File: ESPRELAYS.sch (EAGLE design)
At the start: 52 parts, among them IC1 ESP12SMT, J1 2.1MM DC Jack, K1 HE751, K2 HE751, K3 HE751, K4 HE751, Q1 2N7002, Q2 2N7002, Q3 2N7002, Q4 2N7002

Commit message: Added SIP reed relays
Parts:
- added D5, D6: (no value), SparkFun:DIODESMA
- added H8, H9: (no value), freetronics-jon:M02PTH
- added K5, K6: REED, relay:REED
- K1, K2, K3, K4: value HE751 -> REED; device relay:HE751 -> relay:REED
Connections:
- new net N$15: H8.1, K42.S
- new net N$16: H8.2, K42.P
- new net N$17: H9.1, K62.S
- new net N$18: H9.2, K62.P
- new net OUT5: D5.A, K41.+
- new net OUT6: D6.A, K61.+
- net 5V: now also D5.C, D6.C, K11.-, K21.-, K31.-, K41.-, K51.-, K61.-; no longer K11.1, K21.1, K31.1, K41.1
- net N$12: now also K52.P; no longer K42.S
- net N$13: now also K32.S; no longer K32.P
- net N$14: now also K32.P; no longer K32.S
- net N$3: now also K12.S; no longer K12.P
- net N$5: now also K12.P; no longer K12.S
- net N$6: now also K22.S; no longer K22.P
- net N$8: now also K52.S; no longer K42.P
- net N$9: now also K22.P; no longer K22.S
- net OUT1: now also K51.+; no longer K41.2
- net OUT2: now also K11.+; no longer K11.2
- net OUT3: now also K21.+; no longer K21.2
- net OUT4: now also K31.+; no longer K31.2
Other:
- moved on the sheet: K1, K2, K3, K4

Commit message: Routing for v1.0 release
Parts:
- removed H2: (no value), freetronics-jon:M02PTH
- removed H3: (no value), freetronics-jon:M04PTH
- added JP1: (no value), freetronics-jon:M03PTH
- added LED7, LED8: RED, freetronics-master-v1:LED0603
- added Q5, Q6: 2N7002, freetronics-master-v1:MOSFET-NCHANNELSMD
- added R19, R20, R22, R23: 1K, freetronics-master-v1:RESISTOR0603
- added R21, R5: 10K, freetronics-master-v1:RESISTOR0603
- D1, D2, D3, D4, D5, D6: value (none) -> 1N4004
- LED2: value CH2/RED -> RED
- LED3: value CH3/RED -> RED
- LED4: value CH4/RED -> RED
- LED5: value CH1/RED -> RED
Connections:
- new net N$19: Q5.G, R19.1, R5.2
- new net N$20: LED7.C, R20.1
- new net N$22: Q6.G, R21.2, R22.1
- new net N$26: LED8.C, R23.1
- net 3.3V: now also JP1.2; no longer H2.1, LED2.A, LED3.A, LED4.A, LED5.A
- net 5V: now also JP1.1, LED2.A, LED3.A, LED4.A, LED5.A, LED7.A, LED8.A
- net GND: now also JP1.3, Q5.S, Q6.S, R21.1, R5.1; no longer H2.2
- net GPIO15: now also R22.2
- net GPIO16: now also R19.2
- net OUT1: no longer H3.1
- net OUT2: no longer H3.2
- net OUT3: no longer H3.3
- net OUT4: no longer H3.4
- net OUT5: now also Q5.D, R20.2
- net OUT6: now also Q6.D, R23.2
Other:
- note added: "5"
- note added: "6"
- note added: "Do not place"
- note added: "Output 1: GPIO12 Output 2: GPIO13 Output 3: GPIO14 Output 4: GPIO5 Output 5: GPIO16 Output 6: GPIO15"
- note added: "Output 5"
- note added: "Output 6"
- note added: "SKU: ESPRELAYS"
- note added: "SuperHouse Automation ESP8266 Relays"
- note added: "V1.0 (2019-04-11)"
- note added: "www.superhouse.tv/esprelays"
- note removed: "Output 1: GPIO12 Output 2: GPIO13 Output 3: GPIO14 Output 4: GPIO5"
- note removed: "SKU: ESPREMOTE"
- note removed: "SuperHouse Automation ESP8266 Remote"
- note removed: "Tx Buttons"
- note removed: "V3.1 (2018-03-28)"
- note removed: "www.superhouse.tv/espremote"
- moved on the sheet: D1, D2, D3, D4, D5, D6, H4, H5, H6, H7, H8, H9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

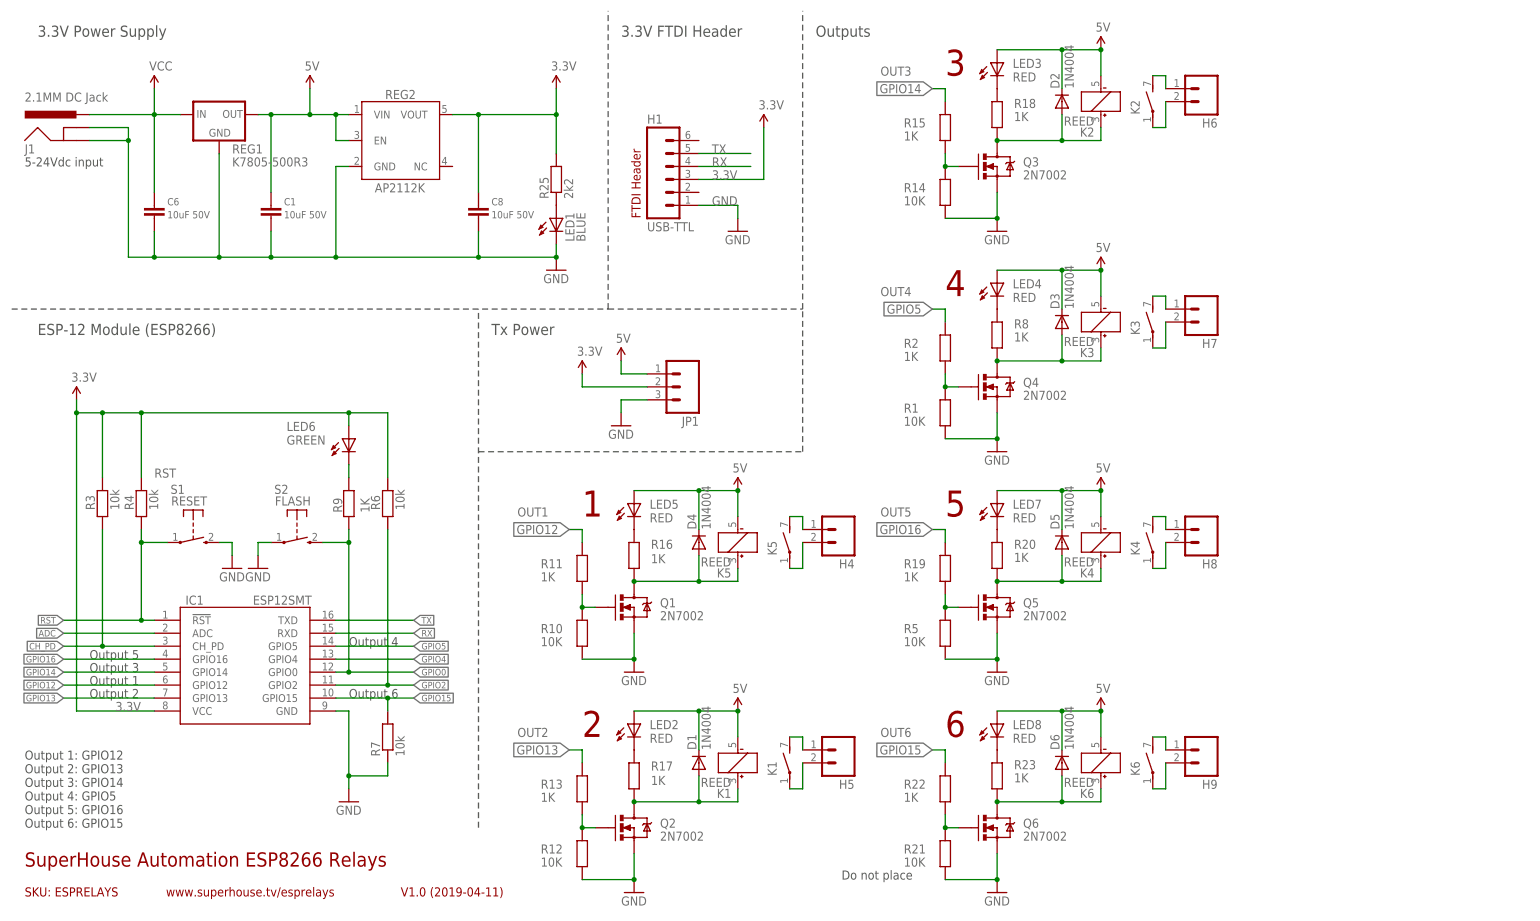
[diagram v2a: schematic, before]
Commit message: Changed output pins to avoid GPIO16 because it pulses on startup. v1.1 release
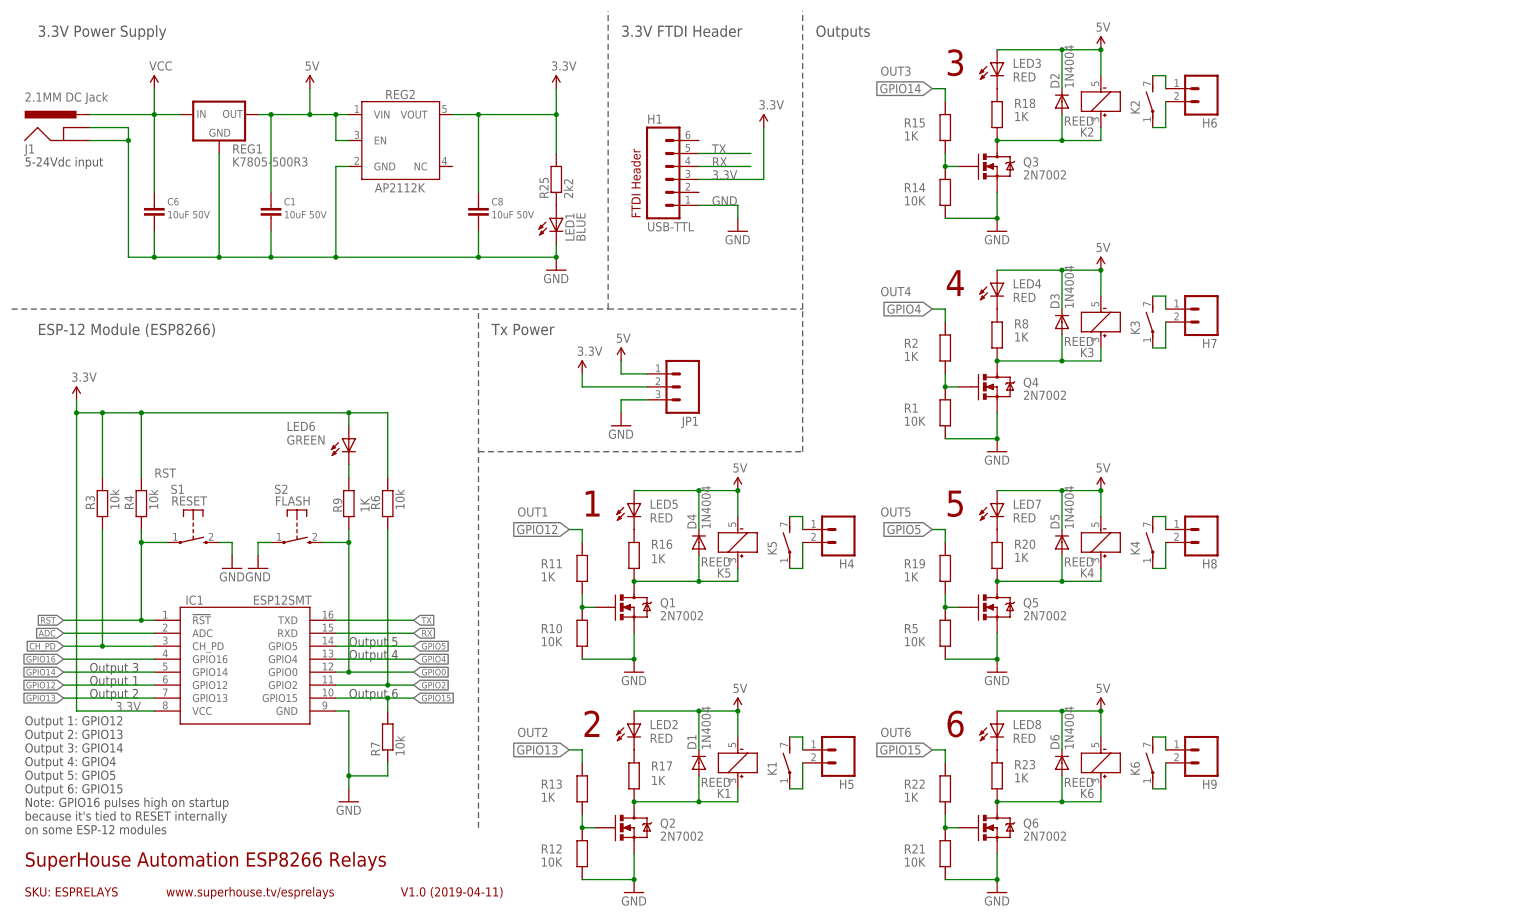
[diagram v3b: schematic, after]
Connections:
- net GPIO16: no longer R19.2
- net GPIO4: now also R2.2
- net GPIO5: now also R19.2; no longer R2.2
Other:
- note added: "Output 1: GPIO12 Output 2: GPIO13 Output 3: GPIO14 Output 4: GPIO4 Output 5: GPIO5 Output 6: GPIO15 Note: GPIO16 pulses high on startup because it's tied to RESET internally on some ESP-12 modules"
- note removed: "Do not place"
- note removed: "Output 1: GPIO12 Output 2: GPIO13 Output 3: GPIO14 Output 4: GPIO5 Output 5: GPIO16 Output 6: GPIO15"
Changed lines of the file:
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@@
 <?xml version="1.0" encoding="utf-8"?>
 <!DOCTYPE eagle SYSTEM "eagle.dtd">
-<eagle version="9.3.1">
+<eagle version="9.3.0">
 <drawing>
 <settings>
-<setting alwaysvectorfont="yes"/>
+<setting alwaysvectorfont="no"/>
 <setting keepoldvectorfont="yes"/>
 <setting verticaltext="up"/>
@@
 <text x="124.46" y="175.26" size="2.1844" layer="97" font="vector" ratio="15">3.3V FTDI Header</text>
 <text x="7.62" y="149.86" size="1.778" layer="97" font="vector" ratio="10">5-24Vdc input</text>
-<text x="7.62" y="20.32" size="1.778" layer="97" font="vector" ratio="10">Output 1: GPIO12
+<text x="7.62" y="19.05" size="1.778" layer="97" font="vector" ratio="10">Output 1: GPIO12
 Output 2: GPIO13
 Output 3: GPIO14
-Output 4: GPIO5
-Output 5: GPIO16
-Output 6: GPIO15</text>
+Output 4: GPIO4
+Output 5: GPIO5
+Output 6: GPIO15
+Note: GPIO16 pulses high on startup
+because it's tied to RESET internally
+on some ESP-12 modules</text>
 <text x="20.32" y="48.26" size="1.778" layer="97">Output 1</text>
 <text x="20.32" y="45.72" size="1.778" layer="97">Output 2</text>
 <text x="20.32" y="50.8" size="1.778" layer="97">Output 3</text>
-<text x="71.12" y="55.88" size="1.778" layer="97">Output 4</text>
+<text x="71.12" y="53.34" size="1.778" layer="97">Output 4</text>
 <text x="187.96" y="81.28" size="5.08" layer="94" ratio="12">5</text>
 <text x="187.96" y="38.1" size="5.08" layer="94" ratio="12">6</text>
-<text x="20.32" y="53.34" size="1.778" layer="97">Output 5</text>
+<text x="71.12" y="55.88" size="1.778" layer="97">Output 5</text>
 <text x="71.12" y="45.72" size="1.778" layer="97">Output 6</text>
 <wire x1="96.52" y1="20.32" x2="96.52" y2="121.92" width="0.254" layer="97" style="longdash"/>
@@
 <wire x1="160.02" y1="93.98" x2="160.02" y2="121.92" width="0.254" layer="97" style="longdash"/>
 <text x="99.06" y="116.84" size="2.1844" layer="97" font="vector" ratio="15">Tx Power</text>
-<text x="167.64" y="10.16" size="1.778" layer="97">Do not place</text>
 </plain>
 <instances>
@@
 </segment>
 <segment>
+<wire x1="187.96" y1="76.2" x2="187.96" y2="78.74" width="0.1524" layer="91"/>
+<wire x1="187.96" y1="78.74" x2="185.42" y2="78.74" width="0.1524" layer="91"/>
+<label x="185.42" y="78.74" size="1.778" layer="95" rot="R180" xref="yes"/>
+<pinref part="R19" gate="G$1" pin="2"/>
+</segment>
+</net>
+<net name="GPIO4" class="0">
+<segment>
+<pinref part="IC1" gate="G$1" pin="GPIO4"/>
+<wire x1="68.58" y1="53.34" x2="83.82" y2="53.34" width="0.1524" layer="91"/>
+<label x="83.82" y="53.34" size="1.27" layer="95" xref="yes"/>
+</segment>
+<segment>
 <pinref part="R2" gate="G$1" pin="2"/>
 <wire x1="187.96" y1="119.38" x2="187.96" y2="121.92" width="0.1524" layer="91"/>
 <wire x1="187.96" y1="121.92" x2="185.42" y2="121.92" width="0.1524" layer="91"/>
 <label x="185.42" y="121.92" size="1.778" layer="95" rot="R180" xref="yes"/>
-</segment>
-</net>
-<net name="GPIO4" class="0">
-<segment>
-<pinref part="IC1" gate="G$1" pin="GPIO4"/>
-<wire x1="68.58" y1="53.34" x2="83.82" y2="53.34" width="0.1524" layer="91"/>
-<label x="83.82" y="53.34" size="1.27" layer="95" xref="yes"/>
 </segment>
 </net>
@@
 <label x="15.24" y="53.34" size="1.27" layer="95" rot="R180" xref="yes"/>
 </segment>
-<segment>
-<wire x1="187.96" y1="76.2" x2="187.96" y2="78.74" width="0.1524" layer="91"/>
-<wire x1="187.96" y1="78.74" x2="185.42" y2="78.74" width="0.1524" layer="91"/>
-<label x="185.42" y="78.74" size="1.778" layer="95" rot="R180" xref="yes"/>
-<pinref part="R19" gate="G$1" pin="2"/>
-</segment>
 </net>

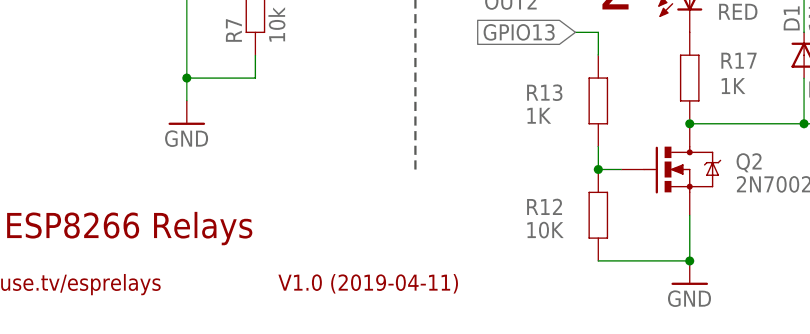
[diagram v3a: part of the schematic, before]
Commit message: Fixed revision number in schematic
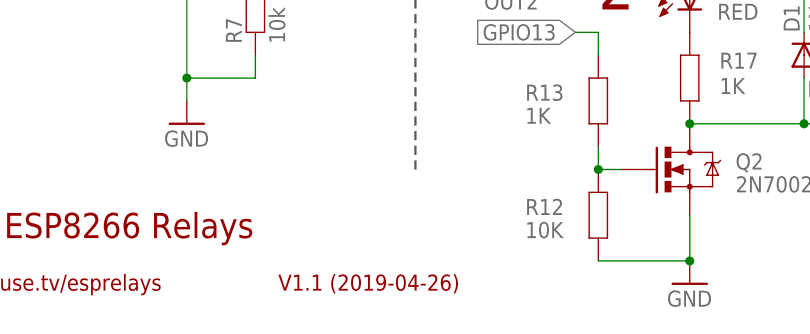
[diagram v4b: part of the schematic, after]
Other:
- note added: "V1.1 (2019-04-26)"
- note removed: "V1.0 (2019-04-11)"
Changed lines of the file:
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@@
 <?xml version="1.0" encoding="utf-8"?>
 <!DOCTYPE eagle SYSTEM "eagle.dtd">
-<eagle version="9.3.0">
+<eagle version="9.4.0">
 <drawing>
 <settings>
@@
 <text x="7.62" y="6.858" size="1.778" layer="94">SKU: ESPRELAYS</text>
 <text x="7.62" y="12.7" size="2.794" layer="94">SuperHouse Automation ESP8266 Relays</text>
-<text x="81.28" y="6.858" size="1.778" layer="94">V1.0 (2019-04-11)</text>
+<text x="81.28" y="6.858" size="1.778" layer="94">V1.1 (2019-04-26)</text>
 <text x="35.306" y="6.858" size="1.778" layer="94">www.superhouse.tv/esprelays</text>
 <frame x1="5.08" y1="5.08" x2="109.22" y2="17.78" columns="0" rows="0" layer="94" border-left="no" border-top="no" border-right="no" border-bottom="no"/>

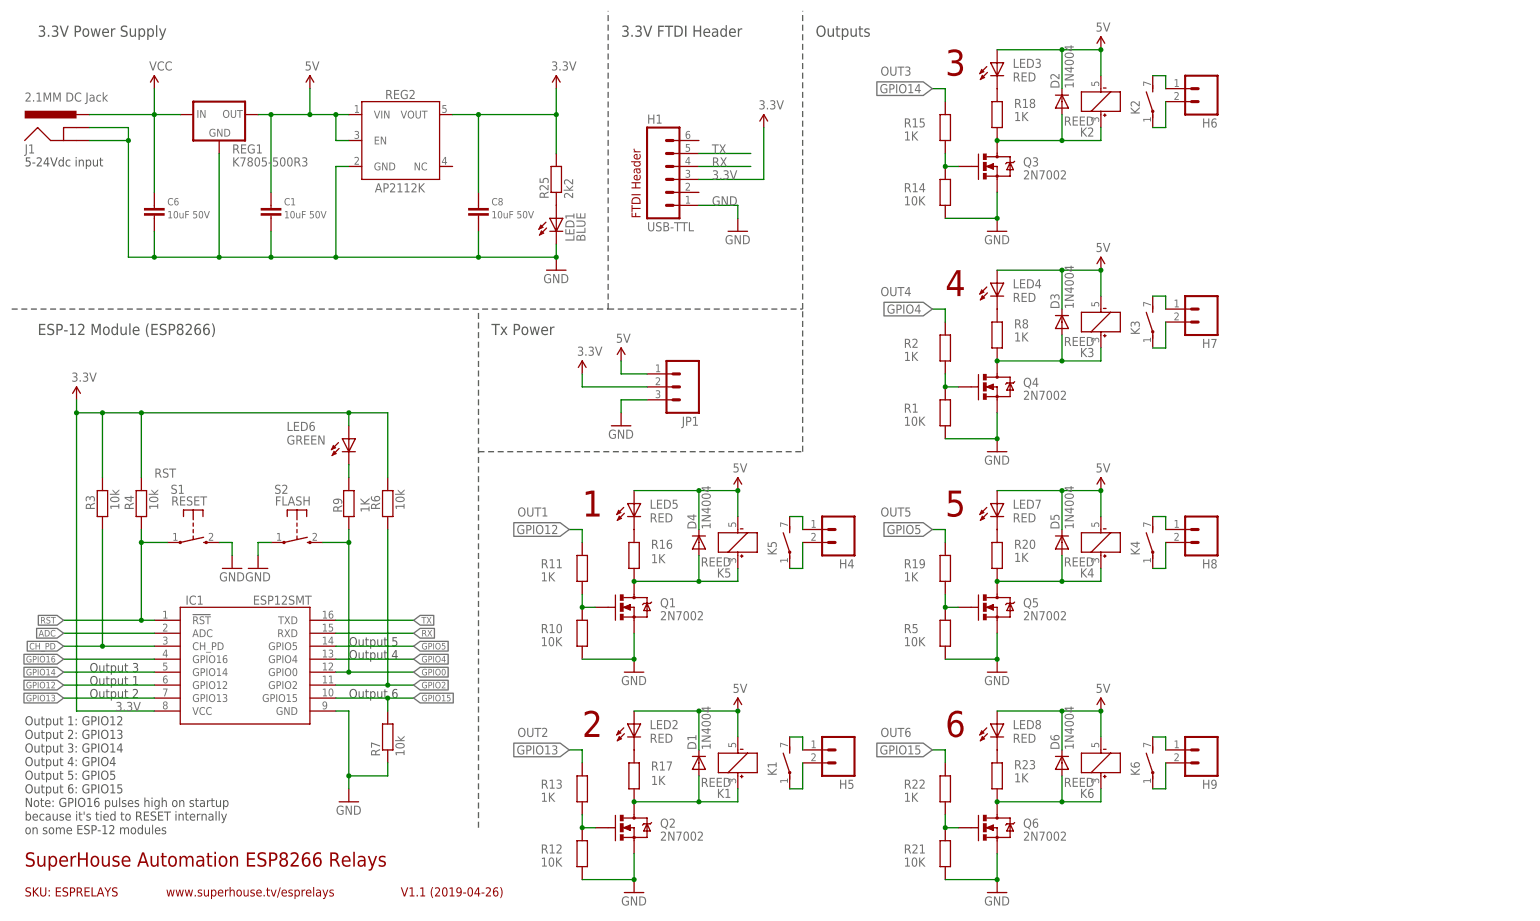
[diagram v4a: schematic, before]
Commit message: Replaced most parts using SuperHouse library to add 3D models
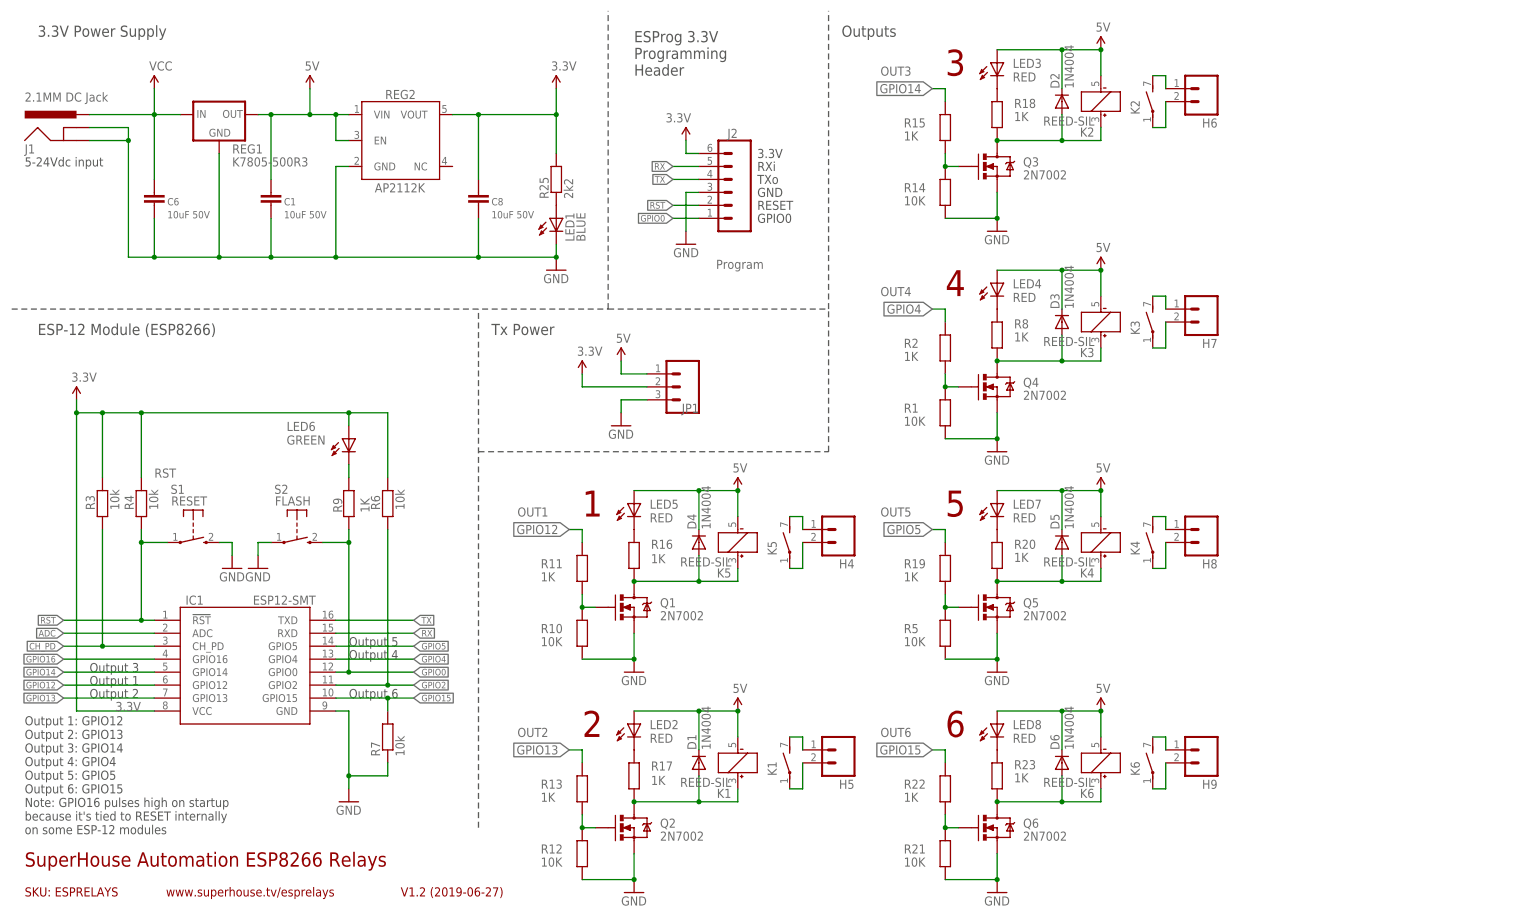
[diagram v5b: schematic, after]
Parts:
- removed H1: USB-TTL, freetronics:M06SIP
- added J2: Program, SuperHouse-Connectors:M06-SOCKET
- C1, C6, C8: device freetronics-jon:C-EUC0805 -> SuperHouse-DiscreteSemi:CAP0805
- D1, D2, D3, D4, D5, D6: device SparkFun:DIODESMA -> SuperHouse-DiscreteSemi:DIODESMA
- H4, H5, H6, H7, H8, H9: device freetronics-jon:M02PTH -> SuperHouse-Connectors:M02-PIN
- IC1: value ESP12SMT -> ESP12-SMT; device freetronics-jon:ESP12SMT -> SuperHouse-MCUs:ESP12-SMT
- J1: device freetronics-jon:POWER_JACKPTH_SLOTS -> SuperHouse-Connectors:POWER_JACK-SLOTS
- JP1: device freetronics-jon:M03PTH -> SuperHouse-Connectors:M03-PLAIN
- K1, K2, K3, K4, K5, K6: value REED -> REED-SIL; device relay:REED -> SuperHouse-Relays:REED-SIL
- LED1: device freetronics-jon:LED0603 -> SuperHouse-LEDs:LED0603
- LED2, LED3, LED4, LED5, LED6, LED7, LED8: device freetronics-master-v1:LED0603 -> SuperHouse-LEDs:LED0603
- Q1, Q2, Q3, Q4, Q5, Q6: device freetronics-master-v1:MOSFET-NCHANNELSMD -> SuperHouse-DiscreteSemi:MOSFET-NCHANNELSMD
- R1, R10, R11, R12, R13, R14, R15, R16, R17, R18, R19, R2, R20, R21, R22, R23, R5, R8, R9: device freetronics-master-v1:RESISTOR0603 -> SuperHouse-DiscreteSemi:RESISTOR0603
- R25, R3, R4, R6, R7: device freetronics-jon:RESISTOR0603 -> SuperHouse-DiscreteSemi:RESISTOR0603
- REG1: device freetronics-jon:K78XX-500R3 -> SuperHouse-Regulators:K78XX-500R3
- REG2: device freetronics-jon:AP2112KSOT25 -> SuperHouse-Regulators:AP2112KSOT25
- S1, S2: device freetronics-jon:TAC_SWITCH_2PINSMT -> SuperHouse-Switches:TAC_SWITCH_2PINSMT
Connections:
- net 3.3V: now also J2.6; no longer H1.3
- net GND: now also J2.3; no longer H1.1
- net GPIO0: now also J2.1
- net RST: now also J2.2
- net RX: now also J2.5; no longer H1.4
- net TX: now also J2.4; no longer H1.5
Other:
- note added: "3.3V"
- note added: "ESProg 3.3V Programming Header"
- note added: "GND"
- note added: "GPIO0"
- note added: "RESET"
- note added: "RXi"
- note added: "TXo"
- note added: "V1.2 (2019-06-27)"
- note removed: "3.3V FTDI Header"
- note removed: "FTDI Header"
- note removed: "V1.1 (2019-04-26)"
- moved on the sheet: C1, C6, C8
